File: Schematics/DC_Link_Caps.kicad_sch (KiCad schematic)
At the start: 19 parts, among them J10 464379202, J11 464369202

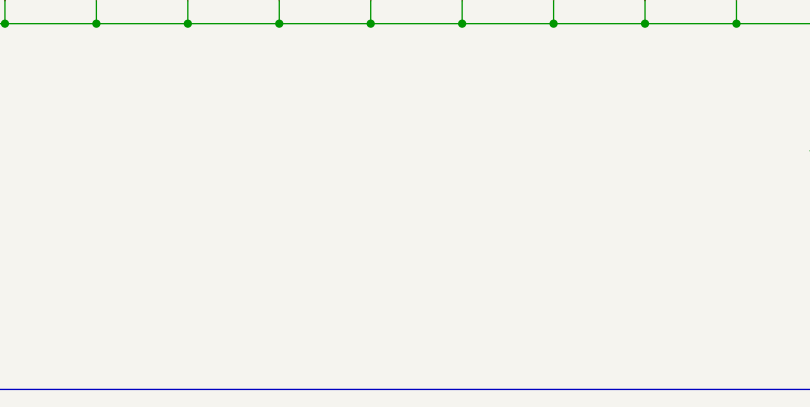
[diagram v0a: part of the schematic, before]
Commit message: Adding Mounting holes for DC Link Caps
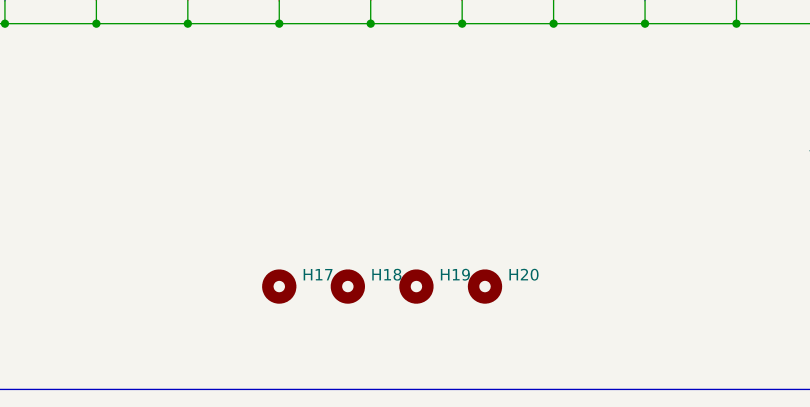
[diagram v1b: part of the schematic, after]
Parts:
- added H17, H18, H19, H20: MountingHole, MountingHole:MountingHole_2.2mm_M2, symbol Mechanical:MountingHole
